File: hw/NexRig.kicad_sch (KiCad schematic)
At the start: 7 parts

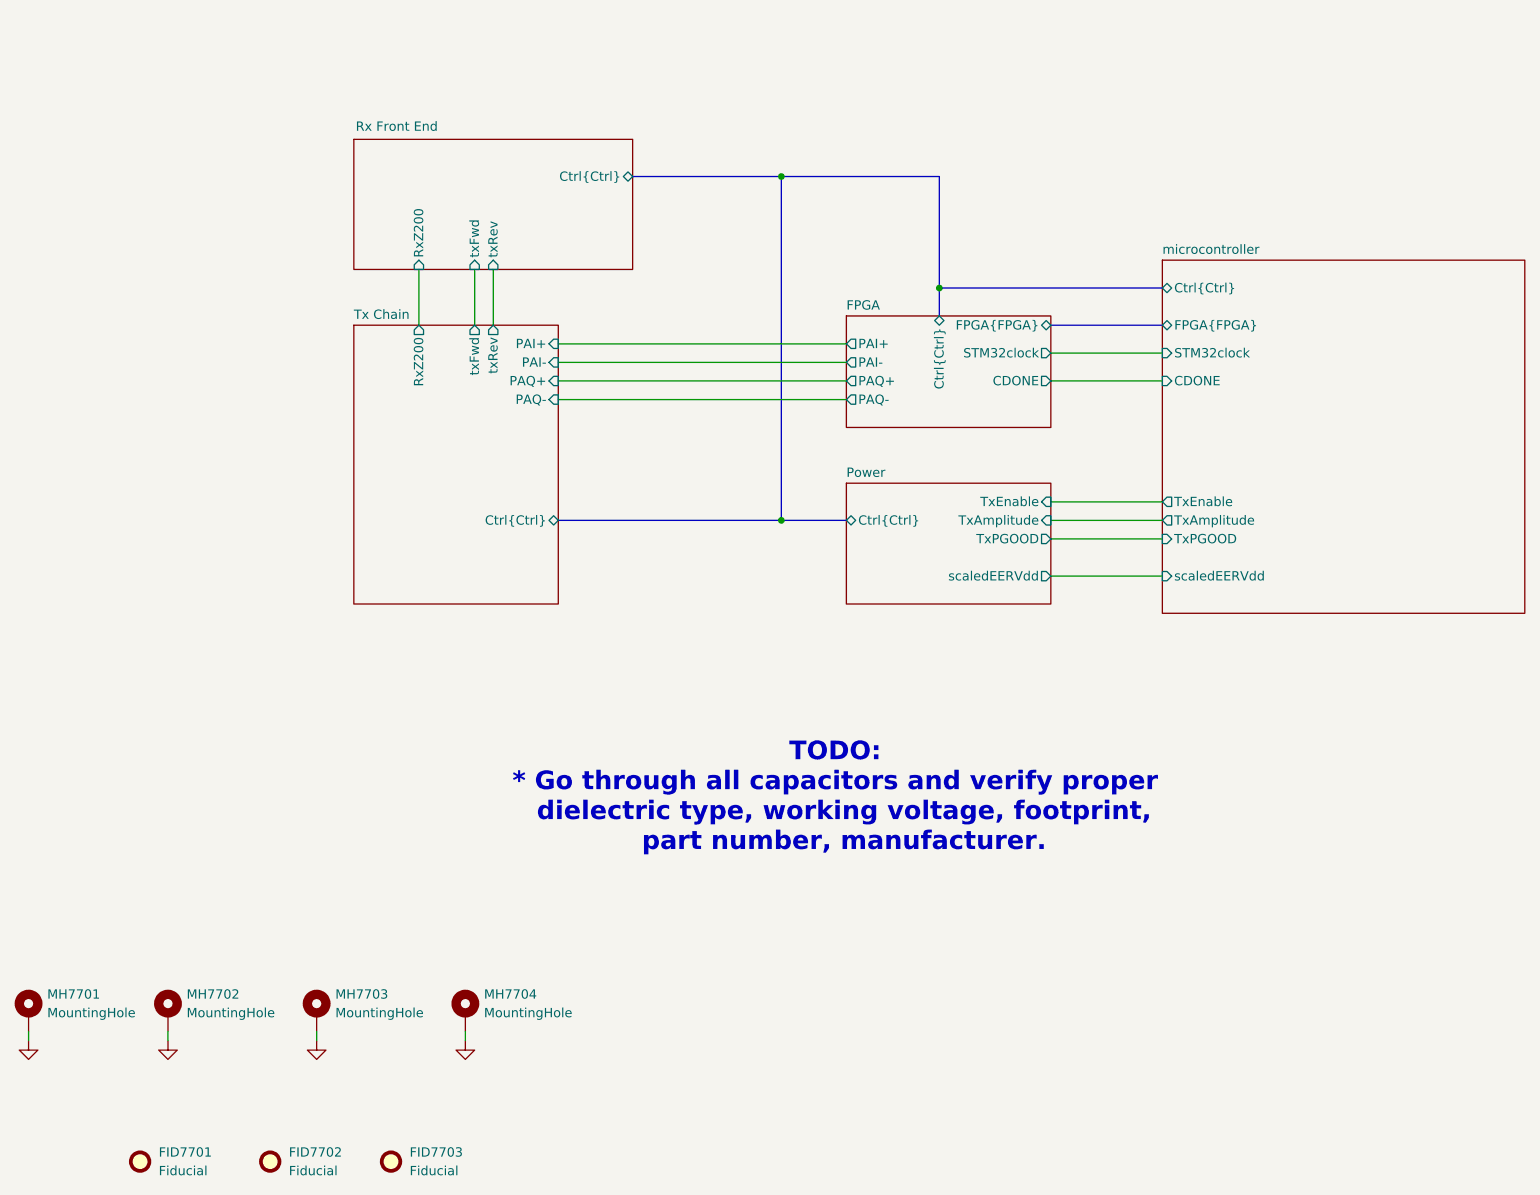
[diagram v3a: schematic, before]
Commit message: Fixed GPIO assignments. Fixed symbol for GRL2-2 relays.
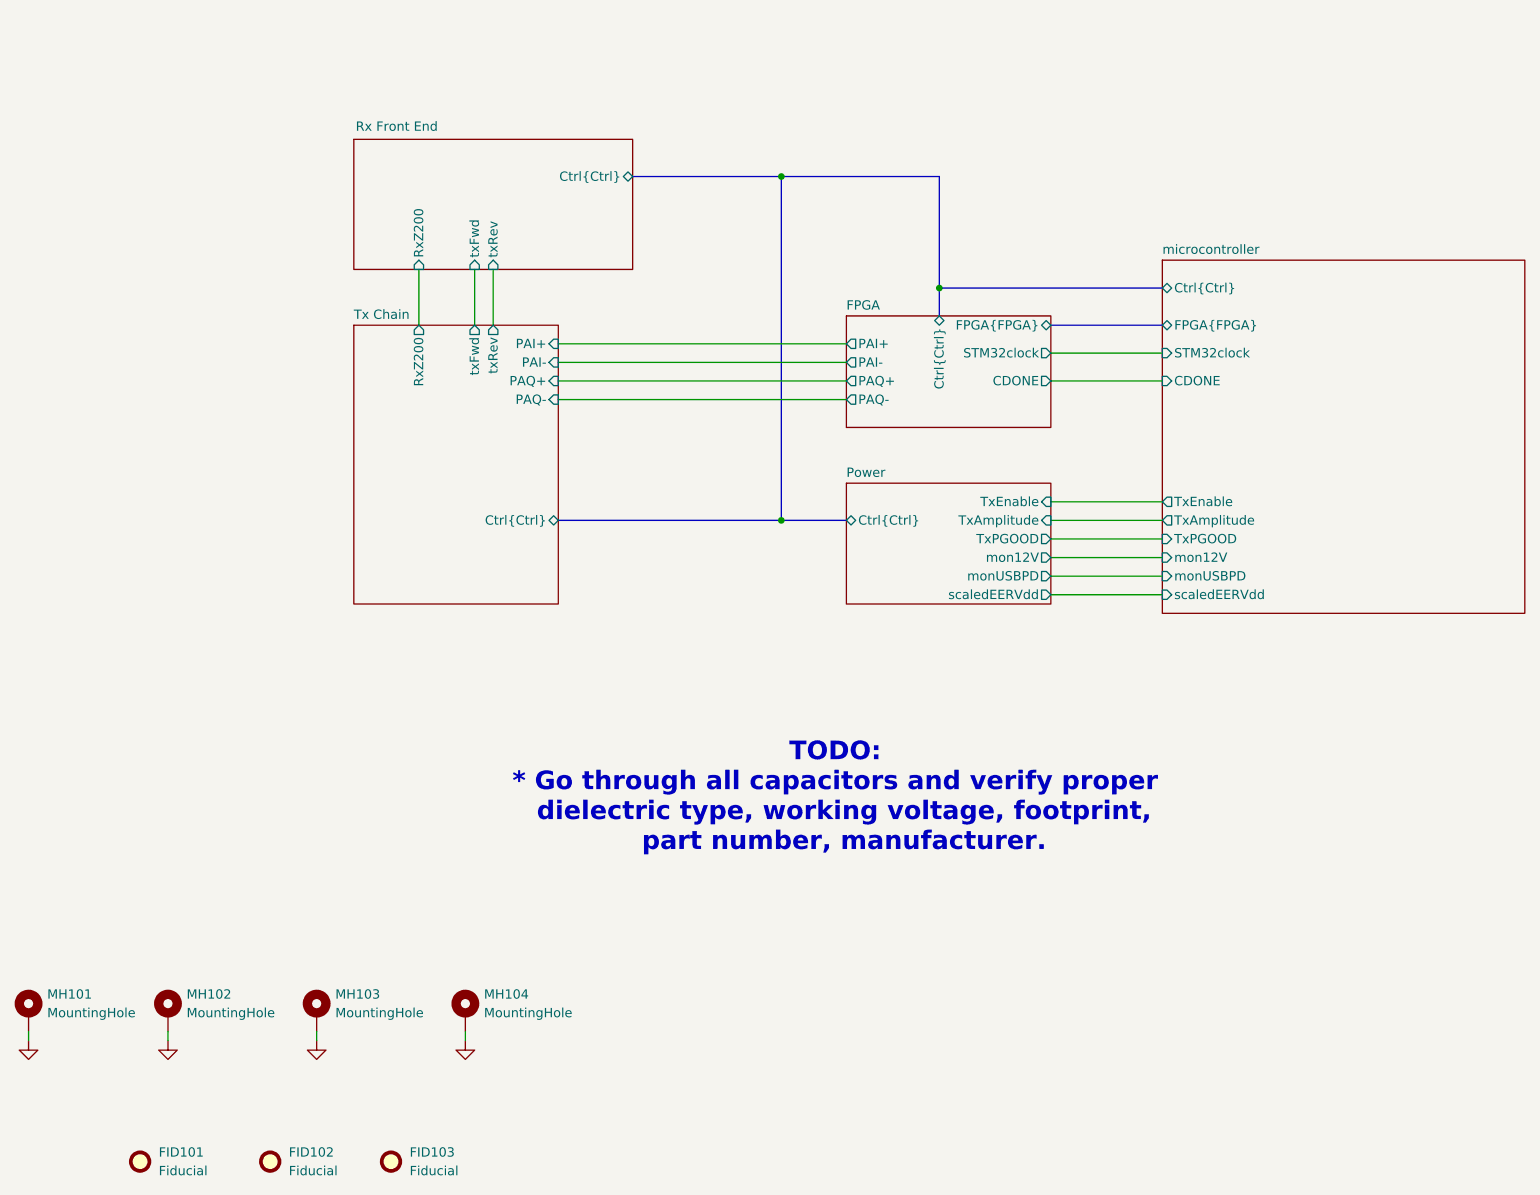
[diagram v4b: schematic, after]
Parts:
- renumbered FID7701 to FID101, FID7702 to FID102, FID7703 to FID103, MH7701 to MH101, MH7702 to MH102, MH7703 to MH103, MH7704 to MH104
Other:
- sheet Power ports: added mon12V, monUSBPD; removed none
- sheet microcontroller ports: added mon12V, monUSBPD; removed none
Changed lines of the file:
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@@
 			"txMCLK" "txWCLK" "usbReset" "usbPOK2" "usbPOK3" "usbnALERT" "enable6V"
 			"enable3VA" "enable5VA" "nTxRelay" "enable3V3" "audioSCL" "audioSDA" "enableFPGA1V2"
-			"enableFPGAIO"
+			"enableFPGAIO" "mon12V"
 		)
 	)
@@
 	(wire
 		(pts
+			(xy 173.99 104.14) (xy 189.23 104.14)
+		)
+		(stroke
+			(width 0)
+			(type default)
+		)
+	)
+	(wire
+		(pts
+			(xy 106.68 72.39) (xy 146.05 72.39)
+		)
+		(stroke
+			(width 0)
+			(type default)
+		)
+	)
+	(wire
+		(pts
+			(xy 173.99 91.44) (xy 189.23 91.44)
+		)
+		(stroke
+			(width 0)
+			(type default)
+		)
+	)
+	(wire
+		(pts
+			(xy 173.99 71.12) (xy 189.23 71.12)
+		)
+		(stroke
+			(width 0)
+			(type default)
+		)
+	)
+	(wire
+		(pts
+			(xy 73.66 163.83) (xy 73.66 165.1)
+		)
+		(stroke
+			(width 0)
+			(type default)
+		)
+	)
+	(bus
+		(pts
+			(xy 137.16 46.99) (xy 158.75 46.99)
+		)
+		(stroke
+			(width 0)
+			(type default)
+		)
+	)
+	(wire
+		(pts
 			(xy 173.99 101.6) (xy 189.23 101.6)
 		)
@@
 	(wire
 		(pts
-			(xy 106.68 72.39) (xy 146.05 72.39)
-		)
-		(stroke
-			(width 0)
-			(type default)
-		)
-	)
-	(wire
-		(pts
-			(xy 173.99 91.44) (xy 189.23 91.44)
-		)
-		(stroke
-			(width 0)
-			(type default)
-		)
-	)
-	(wire
-		(pts
-			(xy 173.99 71.12) (xy 189.23 71.12)
-		)
-		(stroke
-			(width 0)
-			(type default)
-		)
-	)
-	(wire
-		(pts
-			(xy 73.66 163.83) (xy 73.66 165.1)
+			(xy 106.68 69.85) (xy 146.05 69.85)
 		)
 		(stroke
@@
 	(bus
 		(pts
-			(xy 137.16 46.99) (xy 158.75 46.99)
-		)
-		(stroke
-			(width 0)
-			(type default)
-		)
-	)
-	(wire
-		(pts
-			(xy 106.68 69.85) (xy 146.05 69.85)
+			(xy 173.99 67.31) (xy 189.23 67.31)
+		)
+		(stroke
+			(width 0)
+			(type default)
+		)
+	)
+	(wire
+		(pts
+			(xy 95.25 67.31) (xy 95.25 59.69)
+		)
+		(stroke
+			(width 0)
+			(type default)
+		)
+	)
+	(wire
+		(pts
+			(xy 173.99 74.93) (xy 189.23 74.93)
+		)
+		(stroke
+			(width 0)
+			(type default)
+		)
+	)
+	(wire
+		(pts
+			(xy 106.68 77.47) (xy 146.05 77.47)
 		)
 		(stroke
@@
 	(bus
 		(pts
-			(xy 173.99 67.31) (xy 189.23 67.31)
-		)
-		(stroke
-			(width 0)
-			(type default)
-		)
-	)
-	(wire
-		(pts
-			(xy 95.25 67.31) (xy 95.25 59.69)
-		)
-		(stroke
-			(width 0)
-			(type default)
-		)
-	)
-	(wire
-		(pts
-			(xy 173.99 74.93) (xy 189.23 74.93)
-		)
-		(stroke
-			(width 0)
-			(type default)
-		)
-	)
-	(wire
-		(pts
-			(xy 106.68 77.47) (xy 146.05 77.47)
-		)
-		(stroke
-			(width 0)
-			(type default)
-		)
-	)
-	(bus
-		(pts
 			(xy 189.23 62.23) (xy 158.75 62.23)
+		)
+		(stroke
+			(width 0)
+			(type default)
+		)
+	)
+	(wire
+		(pts
+			(xy 173.99 99.06) (xy 189.23 99.06)
 		)
 		(stroke
@@
 		(dnp no)
 		(fields_autoplaced yes)
-		(property "Reference" "FID7702"
+		(property "Reference" "FID102"
 			(at 69.85 180.3399 0)
 			(effects
@@
 			(project "NexRig"
 				(path "/8ae46c04-d01a-4756-8774-512b694bfaff"
-					(reference "FID7702")
+					(reference "FID102")
 					(unit 1)
 				)
@@
 		(dnp no)
 		(fields_autoplaced yes)
-		(property "Reference" "FID7703"
+		(property "Reference" "FID103"
 			(at 86.36 180.3399 0)
 			(effects
@@
 			(project "NexRig"
 				(path "/8ae46c04-d01a-4756-8774-512b694bfaff"
-					(reference "FID7703")
+					(reference "FID103")
 					(unit 1)
 				)
@@
 		(dnp no)
 		(fields_autoplaced yes)
-		(property "Reference" "FID7701"
+		(property "Reference" "FID101"
 			(at 52.07 180.3399 0)
 			(effects
@@
 			(project ""
 				(path "/8ae46c04-d01a-4756-8774-512b694bfaff"
-					(reference "FID7701")
+					(reference "FID101")
 					(unit 1)
 				)
@@
 		(dnp no)
 		(fields_autoplaced yes)
-		(property "Reference" "MH7701"
+		(property "Reference" "MH101"
 			(at 36.83 158.7499 0)
 			(effects
@@
 			(project ""
 				(path "/8ae46c04-d01a-4756-8774-512b694bfaff"
-					(reference "MH7701")
+					(reference "MH101")
 					(unit 1)
 				)
@@
 		(dnp no)
 		(fields_autoplaced yes)
-		(property "Reference" "#PWR07703"
+		(property "Reference" "#PWR0103"
 			(at 73.66 171.45 0)
 			(effects
@@
 			(project "NexRig"
 				(path "/8ae46c04-d01a-4756-8774-512b694bfaff"
-					(reference "#PWR07703")
+					(reference "#PWR0103")
 					(unit 1)
 				)
@@
 		(dnp no)
 		(fields_autoplaced yes)
-		(property "Reference" "#PWR07702"
+		(property "Reference" "#PWR0102"
 			(at 53.34 171.45 0)
 			(effects
@@
 			(project "NexRig"
 				(path "/8ae46c04-d01a-4756-8774-512b694bfaff"
-					(reference "#PWR07702")
+					(reference "#PWR0102")
 					(unit 1)
 				)
@@
 		(dnp no)
 		(fields_autoplaced yes)
-		(property "Reference" "#PWR07704"
+		(property "Reference" "#PWR0104"
 			(at 93.98 171.45 0)
 			(effects
@@
 			(project "NexRig"
 				(path "/8ae46c04-d01a-4756-8774-512b694bfaff"
-					(reference "#PWR07704")
+					(reference "#PWR0104")
 					(unit 1)
 				)
@@
 		(dnp no)
 		(fields_autoplaced yes)
-		(property "Reference" "MH7702"
+		(property "Reference" "MH102"
 			(at 55.88 158.7499 0)
 			(effects
@@
 			(project "NexRig"
 				(path "/8ae46c04-d01a-4756-8774-512b694bfaff"
-					(reference "MH7702")
+					(reference "MH102")
 					(unit 1)
 				)
@@
 		(dnp no)
 		(fields_autoplaced yes)
-		(property "Reference" "MH7703"
+		(property "Reference" "MH103"
 			(at 76.2 158.7499 0)
 			(effects
@@
 			(project "NexRig"
 				(path "/8ae46c04-d01a-4756-8774-512b694bfaff"
-					(reference "MH7703")
+					(reference "MH103")
 					(unit 1)
 				)
@@
 		(dnp no)
 		(fields_autoplaced yes)
-		(property "Reference" "#PWR07701"
+		(property "Reference" "#PWR0101"
 			(at 34.29 171.45 0)
 			(effects
@@
 			(project ""
 				(path "/8ae46c04-d01a-4756-8774-512b694bfaff"
-					(reference "#PWR07701")
+					(reference "#PWR0101")
 					(unit 1)
 				)
@@
 		(dnp no)
 		(fields_autoplaced yes)
-		(property "Reference" "MH7704"
+		(property "Reference" "MH104"
 			(at 96.52 158.7499 0)
 			(effects
@@
 			(project "NexRig"
 				(path "/8ae46c04-d01a-4756-8774-512b694bfaff"
-					(reference "MH7704")
+					(reference "MH104")
 					(unit 1)
 				)
@@
 		)
 		(pin "scaledEERVdd" input
-			(at 189.23 101.6 180)
+			(at 189.23 104.14 180)
 			(effects
 				(font
@@
 		(pin "FPGA{FPGA}" bidirectional
 			(at 189.23 67.31 180)
+			(effects
+				(font
+					(size 1.27 1.27)
+				)
+				(justify left)
+			)
+		)
+		(pin "mon12V" input
+			(at 189.23 99.06 180)
+			(effects
+				(font
+					(size 1.27 1.27)
+				)
+				(justify left)
+			)
+		)
+		(pin "monUSBPD" input
+			(at 189.23 101.6 180)
 			(effects
 				(font
@@
 		)
 		(pin "scaledEERVdd" output
-			(at 173.99 101.6 0)
+			(at 173.99 104.14 0)
 			(effects
 				(font
@@
 			)
 		)
+		(pin "mon12V" output
+			(at 173.99 99.06 0)
+			(effects
+				(font
+					(size 1.27 1.27)
+				)
+				(justify right)
+			)
+		)
+		(pin "monUSBPD" output
+			(at 173.99 101.6 0)
+			(effects
+				(font
+					(size 1.27 1.27)
+				)
+				(justify right)
+			)
+		)

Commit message: I think I have finished the relay conversion and 5V SPI I/O expander crap
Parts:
- renumbered FID101 to FID7701, FID102 to FID7702, FID103 to FID7703, MH101 to MH7701, MH102 to MH7702, MH103 to MH7703, MH104 to MH7704
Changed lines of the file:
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@@
 		(dnp no)
 		(fields_autoplaced yes)
-		(property "Reference" "FID102"
+		(property "Reference" "FID7702"
 			(at 69.85 180.3399 0)
 			(effects
@@
 			(project "NexRig"
 				(path "/8ae46c04-d01a-4756-8774-512b694bfaff"
-					(reference "FID102")
+					(reference "FID7702")
 					(unit 1)
 				)
@@
 		(dnp no)
 		(fields_autoplaced yes)
-		(property "Reference" "FID103"
+		(property "Reference" "FID7703"
 			(at 86.36 180.3399 0)
 			(effects
@@
 			(project "NexRig"
 				(path "/8ae46c04-d01a-4756-8774-512b694bfaff"
-					(reference "FID103")
+					(reference "FID7703")
 					(unit 1)
 				)
@@
 		(dnp no)
 		(fields_autoplaced yes)
-		(property "Reference" "FID101"
+		(property "Reference" "FID7701"
 			(at 52.07 180.3399 0)
 			(effects
@@
 			(project ""
 				(path "/8ae46c04-d01a-4756-8774-512b694bfaff"
-					(reference "FID101")
+					(reference "FID7701")
 					(unit 1)
 				)
@@
 		(dnp no)
 		(fields_autoplaced yes)
-		(property "Reference" "MH101"
+		(property "Reference" "MH7701"
 			(at 36.83 158.7499 0)
 			(effects
@@
 			(project ""
 				(path "/8ae46c04-d01a-4756-8774-512b694bfaff"
-					(reference "MH101")
+					(reference "MH7701")
 					(unit 1)
 				)
@@
 		(dnp no)
 		(fields_autoplaced yes)
-		(property "Reference" "#PWR0103"
+		(property "Reference" "#PWR07703"
 			(at 73.66 171.45 0)
 			(effects
@@
 			(project "NexRig"
 				(path "/8ae46c04-d01a-4756-8774-512b694bfaff"
-					(reference "#PWR0103")
+					(reference "#PWR07703")
 					(unit 1)
 				)
@@
 		(dnp no)
 		(fields_autoplaced yes)
-		(property "Reference" "#PWR0102"
+		(property "Reference" "#PWR07702"
 			(at 53.34 171.45 0)
 			(effects
@@
 			(project "NexRig"
 				(path "/8ae46c04-d01a-4756-8774-512b694bfaff"
-					(reference "#PWR0102")
+					(reference "#PWR07702")
 					(unit 1)
 				)
@@
 		(dnp no)
 		(fields_autoplaced yes)
-		(property "Reference" "#PWR0104"
+		(property "Reference" "#PWR07704"
 			(at 93.98 171.45 0)
 			(effects
@@
 			(project "NexRig"
 				(path "/8ae46c04-d01a-4756-8774-512b694bfaff"
-					(reference "#PWR0104")
+					(reference "#PWR07704")
 					(unit 1)
 				)
@@
 		(dnp no)
 		(fields_autoplaced yes)
-		(property "Reference" "MH102"
+		(property "Reference" "MH7702"
 			(at 55.88 158.7499 0)
 			(effects
@@
 			(project "NexRig"
 				(path "/8ae46c04-d01a-4756-8774-512b694bfaff"
-					(reference "MH102")
+					(reference "MH7702")
 					(unit 1)
 				)
@@
 		(dnp no)
 		(fields_autoplaced yes)
-		(property "Reference" "MH103"
+		(property "Reference" "MH7703"
 			(at 76.2 158.7499 0)
 			(effects
@@
 			(project "NexRig"
 				(path "/8ae46c04-d01a-4756-8774-512b694bfaff"
-					(reference "MH103")
+					(reference "MH7703")
 					(unit 1)
 				)
@@
 		(dnp no)
 		(fields_autoplaced yes)
-		(property "Reference" "#PWR0101"
+		(property "Reference" "#PWR07701"
 			(at 34.29 171.45 0)
 			(effects
@@
 			(project ""
 				(path "/8ae46c04-d01a-4756-8774-512b694bfaff"
-					(reference "#PWR0101")
+					(reference "#PWR07701")
 					(unit 1)
 				)
@@
 		(dnp no)
 		(fields_autoplaced yes)
-		(property "Reference" "MH104"
+		(property "Reference" "MH7704"
 			(at 96.52 158.7499 0)
 			(effects
@@
 			(project "NexRig"
 				(path "/8ae46c04-d01a-4756-8774-512b694bfaff"
-					(reference "MH104")
-					(unit 1)
-				)
+					(reference "MH7704")
+					(unit 1)
+				)
